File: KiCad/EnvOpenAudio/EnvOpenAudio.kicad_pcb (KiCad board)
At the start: 2 copper layers, 21.3 x 68.7 mm, 69 parts, among them J1 USB_C_Receptacle_USB2.0, J2 SM03B-SRSS-TB, J3 Conn_01x10, SW1 B3U-1000, SW2 B3U-1000, U1 W25Q16JVUXIQ, U2 TPS63001DRCR, U3 TLV75518PDBV, U4 RP2350_60QFN, U5 TLV320AIC3100, Y1 ABM8-272-T3

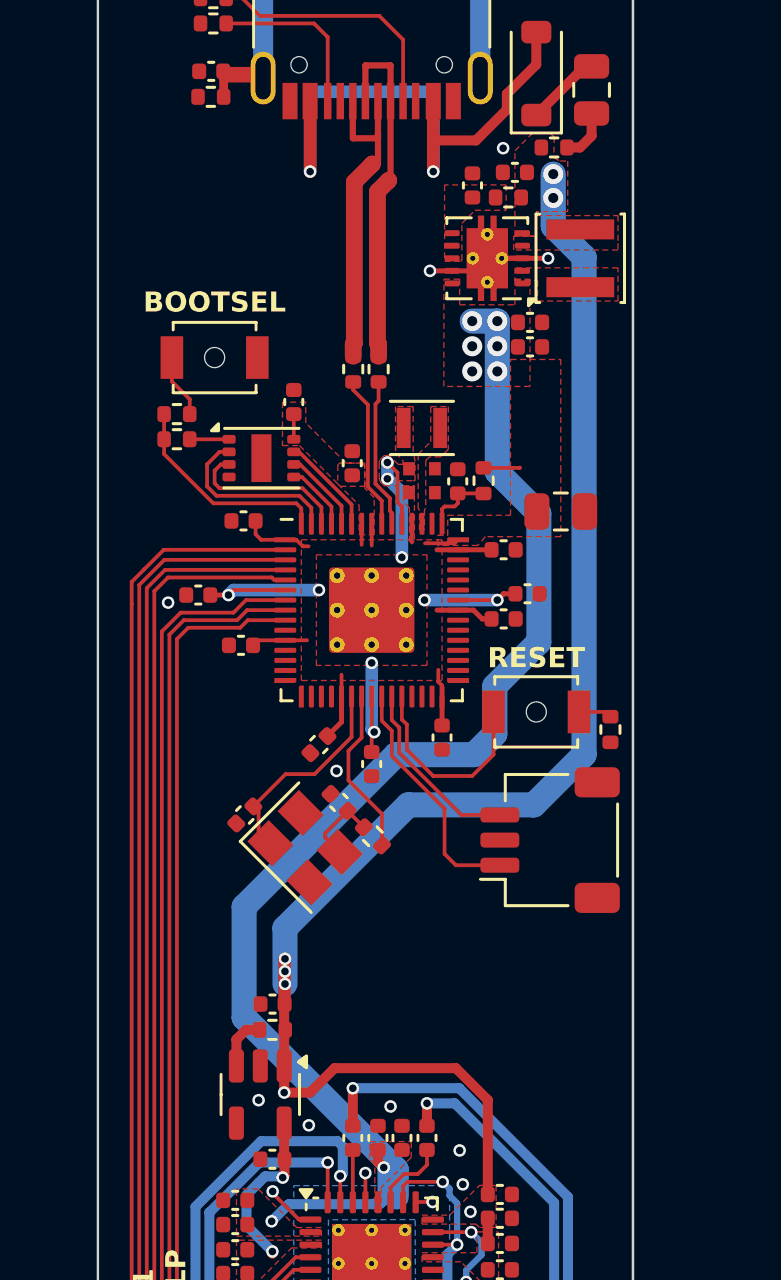
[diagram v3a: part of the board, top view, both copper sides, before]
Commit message: added test pads, swapped inductors for smaller models
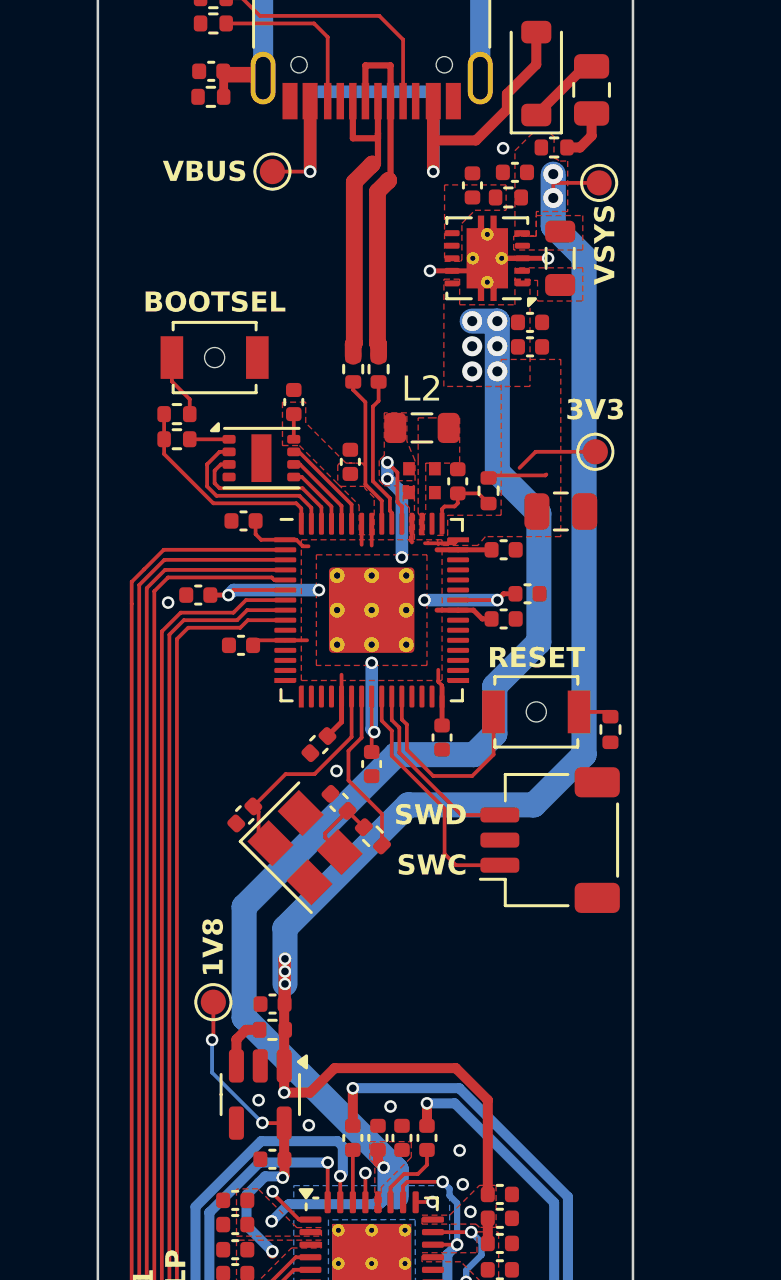
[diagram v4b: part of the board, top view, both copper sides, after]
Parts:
- added TP1: TestPoint, TestPoint:TestPoint_Pad_D1.0mm, F.Cu at (62.0, 40.5)
- added TP2: TestPoint, TestPoint:TestPoint_Pad_D1.0mm, F.Cu at (75.0, 41.0)
- added TP3: TestPoint, TestPoint:TestPoint_Pad_D1.0mm, F.Cu at (59.7, 73.6)
- added TP4: TestPoint, TestPoint:TestPoint_Pad_D1.0mm, F.Cu at (74.9, 51.7)
- L1: value SPH3015H2R2MT -> MPL2016S2R2NHT; footprint Inductor_SMD:L_Sunlord_SWPA3015S -> Inductor_SMD:L_0805_2012Metric
- L2: value 3.3uf 2016 -> MPL2012S3R3MHT; footprint Inductor_SMD:L_Murata_DFE201610P -> Inductor_SMD:L_0805_2012Metric
- moved L1 0.80 mm to (73.5, 44.0)
- moved R10 0.45 mm to (70.7, 53.2)
- moved C17 0.09 mm to (65.2, 52.1)
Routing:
- net +1V8: track 6.75 -> 13.3 mm, vias 2 -> 4
- net +3V3: track 75.0 -> 79.2 mm
- net VSYS: track 59.7 -> 62.1 mm
- net VBUS: track 25.1 -> 26.6 mm
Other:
- board text added: "1V8"
- board text added: "3V3"
- board text added: "SWC"
- board text added: "SWD"
- board text added: "VBUS"
- board text added: "VSYS"

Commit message: changed some component sizes, values ,added seperate analogue ground with small stitching to digital ground.
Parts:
- removed C25, C26, C33, C34: 0.1mF 0402, Capacitor_SMD:C_0402_1005Metric
- C27, C32: value 10mF 0402 -> 10uF 0402
- C28, C30: value 0.1mF 0402 -> 10uF 0402
- C29, C31: value 10mF 0402 -> 100nF 0402
- C35, C36: value 47mF 0402 -> 47uF 0805; footprint Capacitor_SMD:C_0402_1005Metric -> Capacitor_SMD:C_0805_2012Metric
- C37, C38: value 22mF 0402 -> 100nF 0402
- C39, C40: value 1mF 0402 -> 1uF 0402
- moved C36 1.01 mm to (64.8, 78.1)
- moved C35 0.90 mm to (68.7, 78.2)
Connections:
- net MIC1LM renamed MIC1LN
- net SPKM renamed SPKN
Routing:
- net GND: track 13.1 -> 33.1 mm, vias 14 -> 15
- net VSYS: track 62.1 -> 67.6 mm
- net MIC1LP: track 7.16 -> 9.04 mm
- net HPLO: track 22.7 -> 23.9 mm
- net SPKP: track 20.4 -> 21.4 mm
- net HPRO: track 30.0 -> 29.0 mm
- net Net-(U5-HPL): track 2.99 -> 3.67 mm
- net Net-(U5-HPR): track 2.07 -> 2.59 mm
